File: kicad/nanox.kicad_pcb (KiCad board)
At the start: 4 copper layers, 61.7 x 15.9 mm, 138 parts, among them P1 likely an ESD protection diod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, P2 likely an ESD protection diod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, P3 likely an ESD protection diod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, P4 likely an ESD protection diod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, P5 likely an ESD protection diod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, SW1 push button, left, SW2 push button, right, X1 ?, X10 unknown, marked 1C4F, likely 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, X2 unknown, marked 2GC, X3 unknown, marked 6, X4 ?, X5 ?, X6 ?, X7 ?, X8 ?, X9 unknown, marked P8W 26, Y1 crystal, likely the 32 MHz HSE

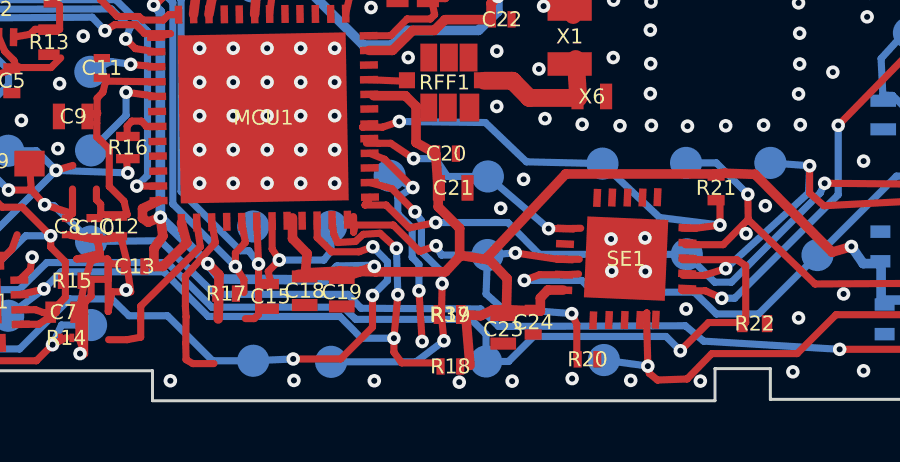
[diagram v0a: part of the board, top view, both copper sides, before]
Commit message: Remove R37, a duplicate of R19
R37 was added by hand on the resistor below R18, which the automatic
pass had already found as R19. R19 keeps R37's better-fitting box.

Co-Authored-By: Claude Opus 5.5 <noreply@anthropic.com>
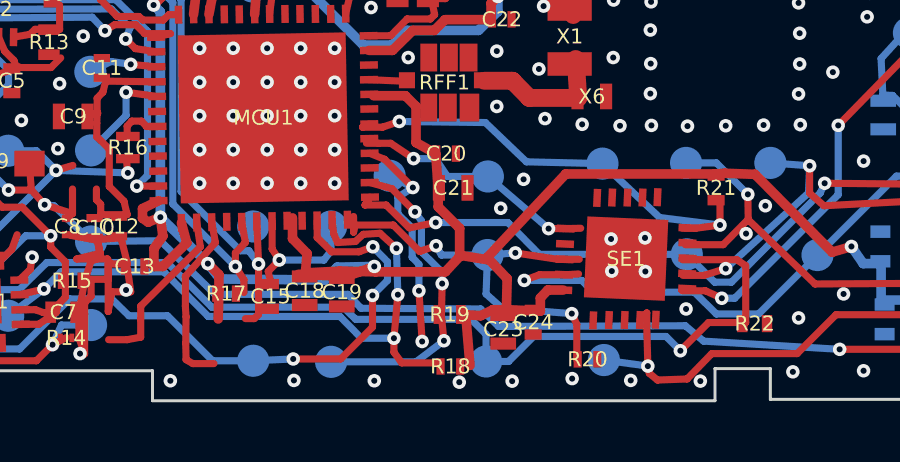
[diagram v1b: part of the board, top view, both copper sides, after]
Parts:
- removed R37: R, 

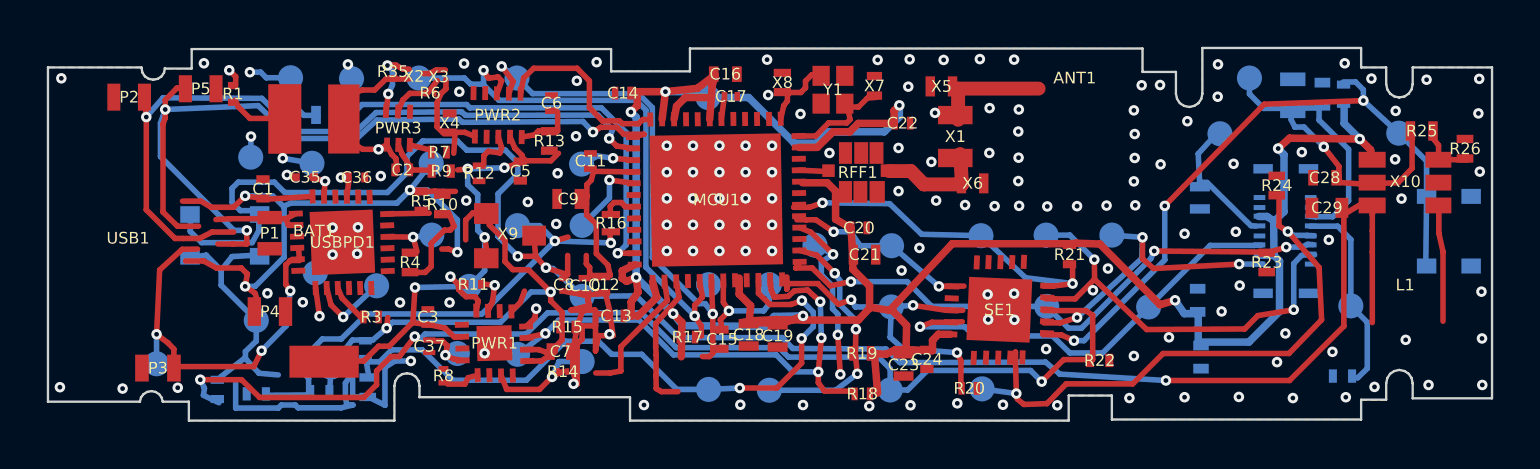
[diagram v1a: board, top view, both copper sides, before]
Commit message: Connect C14, C7, R9 and R13 to the traces over them
They were flagged as overlaps but the traces really end on them: the
+3.3V rail on C14, trace 38 on C7, and trace 41 on R9 and R13.

Co-Authored-By: Claude Opus 5.5 <noreply@anthropic.com>
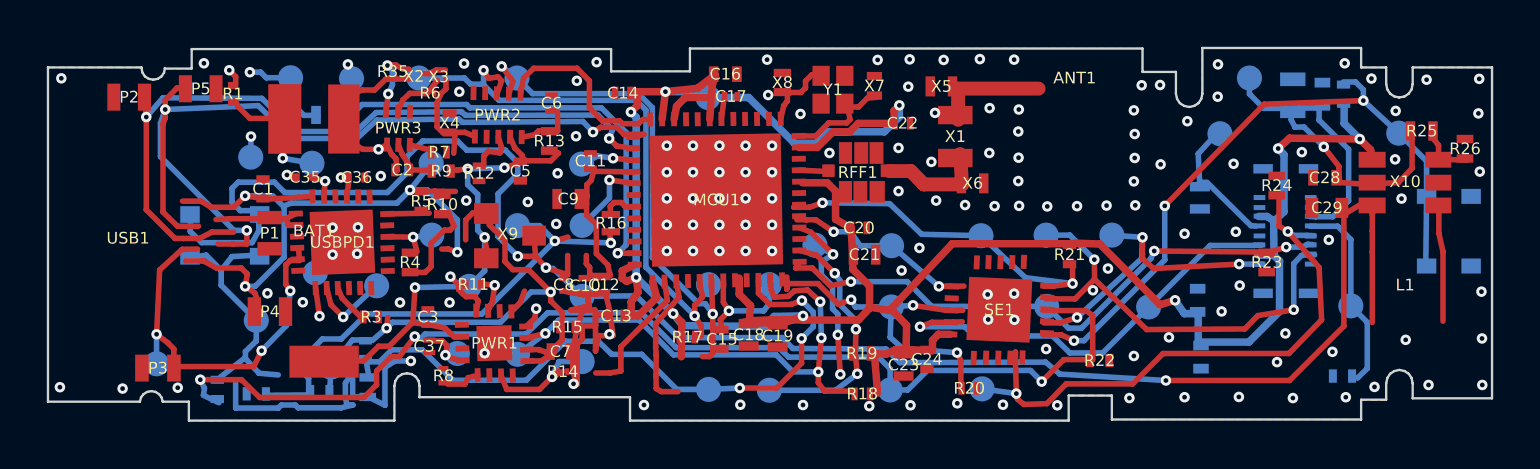
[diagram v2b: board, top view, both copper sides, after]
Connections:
- C14 pad 2: (no net) -> +3.3V rail
- C7 pad 1: (no net) -> Net-T38
- R13 pad 1: (no net) -> Net-T41
- R9 pad 2: (no net) -> Net-T41
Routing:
- net Net-T41: track 22.0 -> 22.7 mm

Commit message: Clear trace 68 from R11 and R12 from its via
Trace 68 now makes one 45-degree run past R11, at the 14 px width of
the real copper, instead of hugging R11's end. R12's box moves onto its
real pads, clear of the trace 41 via, with its GND pin moved along.

Co-Authored-By: Claude Opus 5.5 <noreply@anthropic.com>
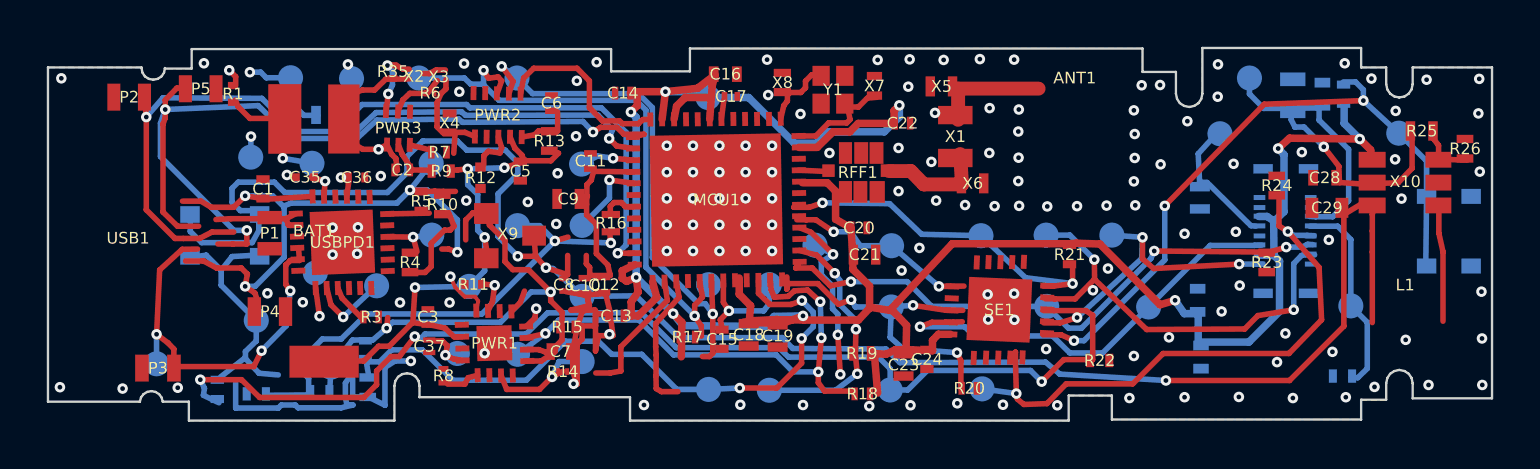
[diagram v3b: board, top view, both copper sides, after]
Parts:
- moved R12 0.20 mm to (19.7, 16.8)

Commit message: Connect trace 65 to R13
Trace 65 ran through R13's free end without a point on it; it does
connect there, so the run gets a point on the pad.

Co-Authored-By: Claude Opus 5.5 <noreply@anthropic.com>
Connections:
- R13 pad 2: (no net) -> Net-T65

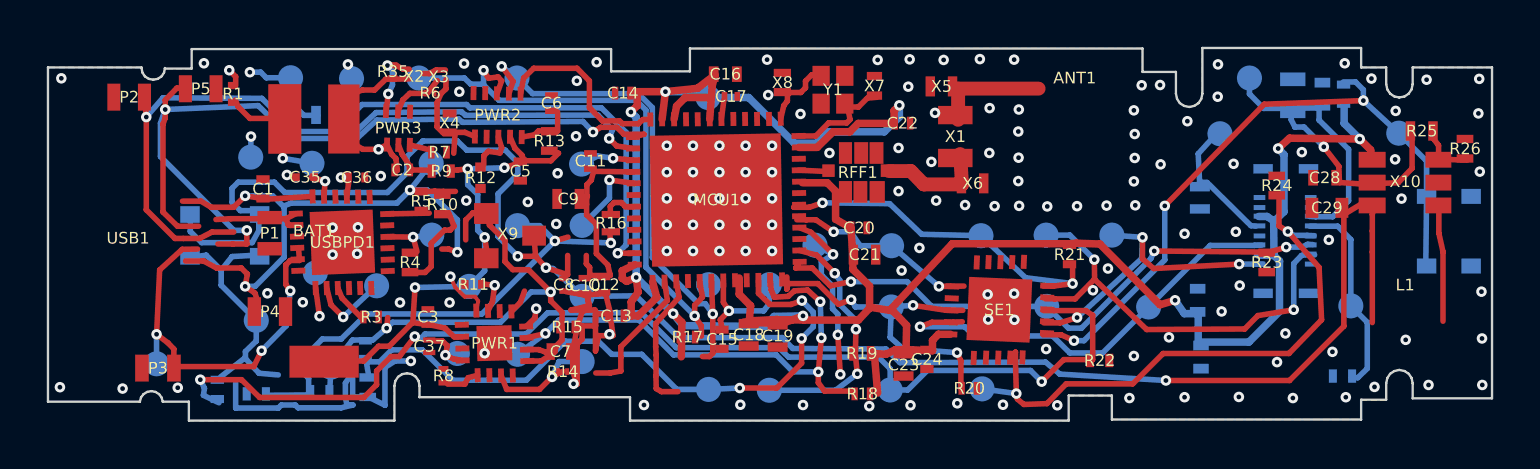
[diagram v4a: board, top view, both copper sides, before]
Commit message: Resize R14 so it joins trace 37 and GND
R14's box only covered its dark body; at its real size the trace 37
branch lands on its left end, and its right end goes to ground.

Co-Authored-By: Claude Opus 5.5 <noreply@anthropic.com>
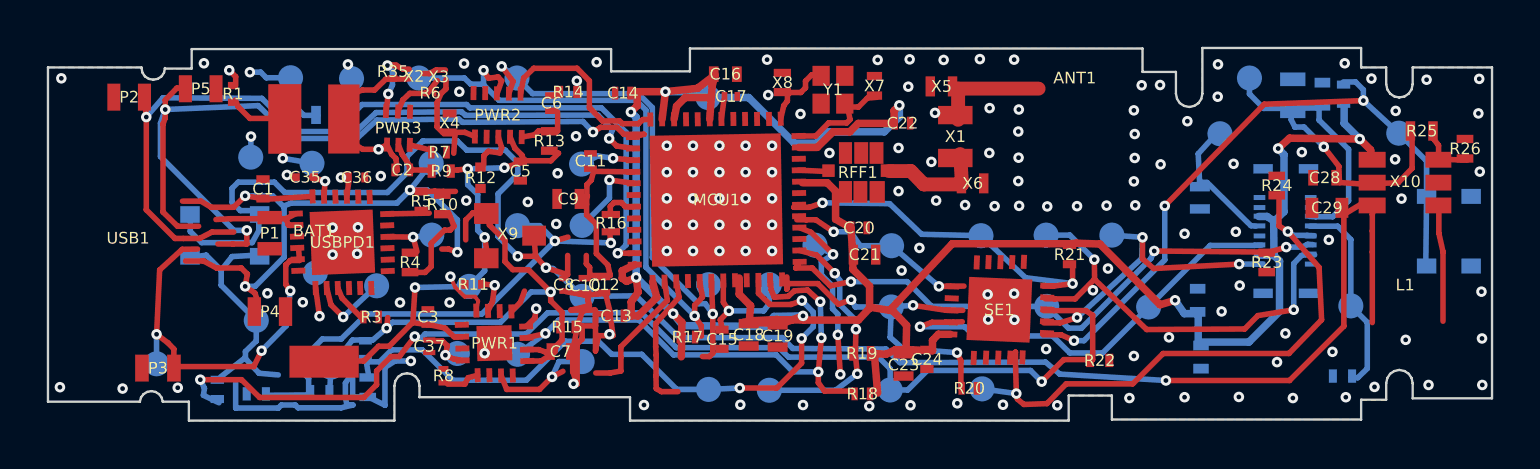
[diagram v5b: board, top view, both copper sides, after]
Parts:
- moved R14 12.0 mm to (23.4, 13.1)

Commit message: Fix R14's position and connect R19 to the +3.3V rail
The previous commit put R14's box 1000 px too low by a typo, leaving it
unconnected; it now sits on its real pads, joining trace 37 and GND.
R19's right end gets a stub from the +3.3V rail, whose bend sat
exactly on the pad's edge.

Co-Authored-By: Claude Opus 5.5 <noreply@anthropic.com>
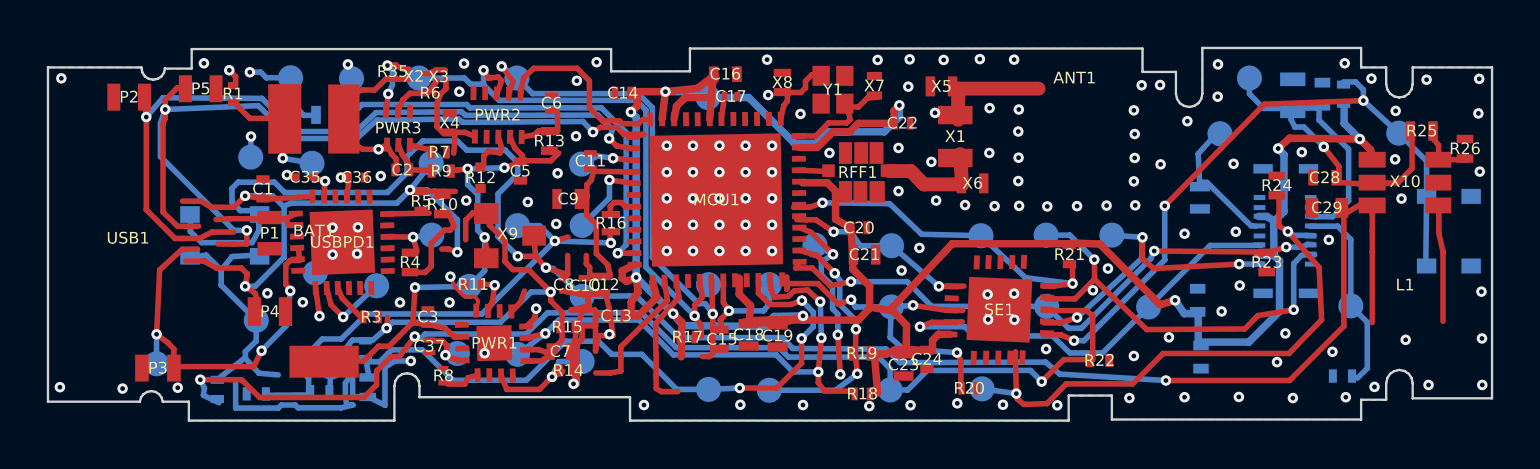
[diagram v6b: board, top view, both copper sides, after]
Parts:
- moved R14 11.9 mm to (23.4, 25.0)
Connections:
- R14 pad 1: (no net) -> Net-T37
- R14 pad 2: (no net) -> GND
- R19 pad 2: (no net) -> +3.3V rail

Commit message: Trace the PD SCL via to TP05
The back-side copper from the PD SCL via reaches TP05, replacing the
stand-in pin that linked them.

Co-Authored-By: Claude Opus 5.5 <noreply@anthropic.com>
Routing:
- net PD SCL: track 1.21 -> 3.07 mm
